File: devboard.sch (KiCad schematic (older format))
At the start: 91 parts, among them J1 Conn_01x04, J2 Conn_02x05_Odd_Even, J3 USB_B_Micro, J4 Conn_01x04, J5 Conn_02x10_Counter_Clockwise, J6 Conn_02x04_Counter_Clockwise, Q1 Q_NPN_BEC, Q2 Q_NPN_BEC, SW1 SW_SPST, U1 ATmega128L-8AU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

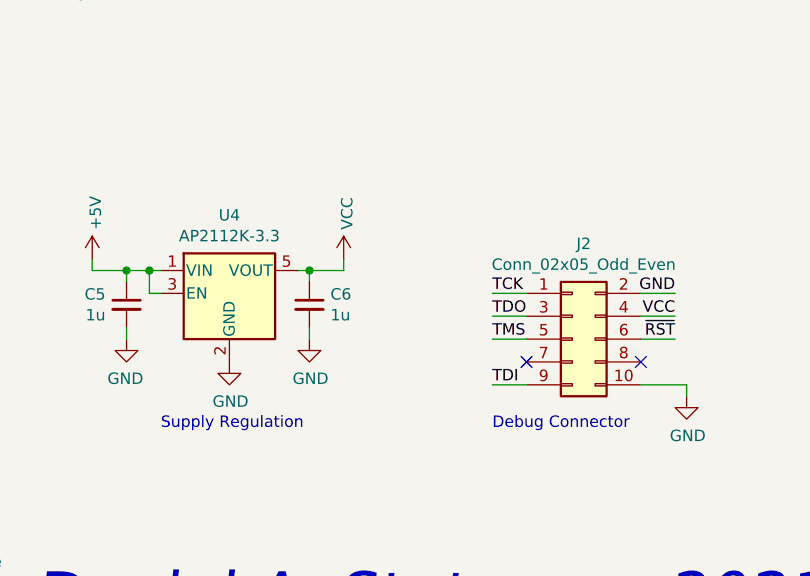
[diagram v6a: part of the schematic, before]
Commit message: Add power indicator and improve silk
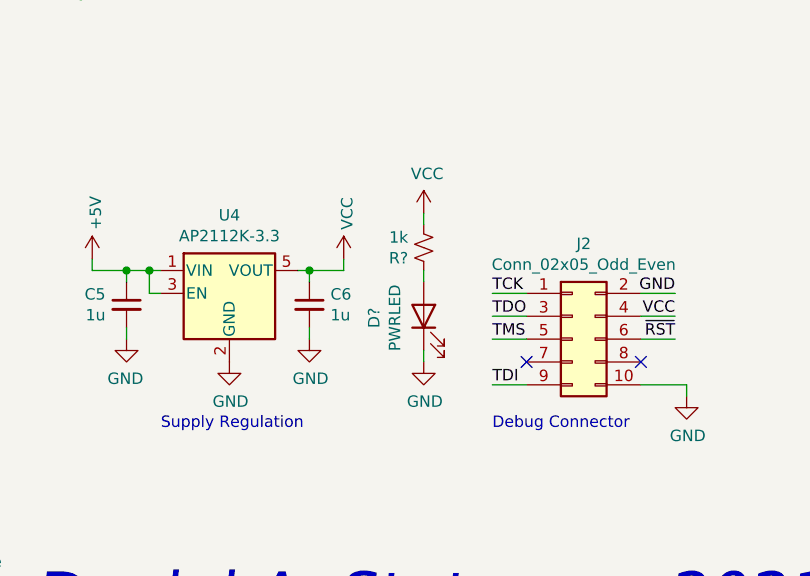
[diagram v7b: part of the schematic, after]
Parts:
- added D?: PWRLED, LED_SMD:LED_0603_1608Metric_Castellated, symbol Device:LED
- added R?: 1k, Resistor_SMD:R_0603_1608Metric_Pad0.98x0.95mm_HandSolder, symbol Device:R_Small_US
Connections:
- net GND: now also D?.1 (K)
- net VCC: now also R?.2
- new net: D?.2 (A), R?.1
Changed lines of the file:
@@
 Wire Wire Line
 	7850 4700 7850 4850
+Connection ~ 7850 4850
+Wire Wire Line
+	7850 4850 8200 4850
+$Comp
+L Device:R_Small_US R?
+U 1 1 60218294
+P 13600 8750
+F 0 "R?" H 13668 8796 50  0000 L CNN
+F 1 "1k" H 13668 8705 50  0000 L CNN
+F 2 "Resistor_SMD:R_0603_1608Metric_Pad0.98x0.95mm_HandSolder" H 13600 8750 50  0001 C CNN
+F 3 "~" H 13600 8750 50  0001 C CNN
+	1    13600 8750
+	-1   0    0    1
+$EndComp
+$Comp
+L power:GND #PWR?
+U 1 1 6028ABB4
+P 13600 9250
+F 0 "#PWR?" H 13600 9000 50  0001 C CNN
+F 1 "GND" H 13605 9077 50  0000 C CNN
+F 2 "" H 13600 9250 50  0001 C CNN
+F 3 "" H 13600 9250 50  0001 C CNN
+	1    13600 9250
+	1    0    0    -1
+$EndComp
+$Comp
+L Device:LED D?
+U 1 1 6021828E
+P 13600 9050
+F 0 "D?" H 13593 9267 50  0000 C CNN
+F 1 "PWRLED" H 13593 9176 50  0000 C CNN
+F 2 "LED_SMD:LED_0603_1608Metric_Castellated" H 13600 9050 50  0001 C CNN
+F 3 "~" H 13600 9050 50  0001 C CNN
+	1    13600 9050
+	0    -1   -1   0
+$EndComp
+Wire Wire Line
+	13600 9200 13600 9250
+Wire Wire Line
+	13600 8850 13600 8900
+$Comp
+L power:VCC #PWR?
+U 1 1 6053403F
+P 13600 8600
+F 0 "#PWR?" H 13600 8450 50  0001 C CNN
+F 1 "VCC" H 13615 8773 50  0000 C CNN
+F 2 "" H 13600 8600 50  0001 C CNN
+F 3 "" H 13600 8600 50  0001 C CNN
+	1    13600 8600
+	1    0    0    -1
+$EndComp
+Wire Wire Line
+	13600 8600 13600 8650
 Wire Bus Line
 	11700 10350 11700 10750
@@
 Wire Bus Line
 	8200 5450 8200 7500
-Connection ~ 7850 4850
-Wire Wire Line
-	7850 4850 8200 4850
 $EndSCHEMATC

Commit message: Annotation update
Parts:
- gave numbers to parts that had none: 2
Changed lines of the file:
@@
 	7850 4850 8200 4850
 $Comp
-L Device:R_Small_US R?
+L Device:R_Small_US R13
 U 1 1 60218294
 P 13600 8750
-F 0 "R?" H 13668 8796 50  0000 L CNN
+F 0 "R13" H 13668 8796 50  0000 L CNN
 F 1 "1k" H 13668 8705 50  0000 L CNN
 F 2 "Resistor_SMD:R_0603_1608Metric_Pad0.98x0.95mm_HandSolder" H 13600 8750 50  0001 C CNN
@@
 $EndComp
 $Comp
-L power:GND #PWR?
+L power:GND #PWR0122
 U 1 1 6028ABB4
 P 13600 9250
-F 0 "#PWR?" H 13600 9000 50  0001 C CNN
+F 0 "#PWR0122" H 13600 9000 50  0001 C CNN
 F 1 "GND" H 13605 9077 50  0000 C CNN
 F 2 "" H 13600 9250 50  0001 C CNN
@@
 $EndComp
 $Comp
-L Device:LED D?
+L Device:LED D11
 U 1 1 6021828E
 P 13600 9050
-F 0 "D?" H 13593 9267 50  0000 C CNN
+F 0 "D11" H 13593 9267 50  0000 C CNN
 F 1 "PWRLED" H 13593 9176 50  0000 C CNN
 F 2 "LED_SMD:LED_0603_1608Metric_Castellated" H 13600 9050 50  0001 C CNN
@@
 	13600 8850 13600 8900
 $Comp
-L power:VCC #PWR?
+L power:VCC #PWR0124
 U 1 1 6053403F
 P 13600 8600
-F 0 "#PWR?" H 13600 8450 50  0001 C CNN
+F 0 "#PWR0124" H 13600 8450 50  0001 C CNN
 F 1 "VCC" H 13615 8773 50  0000 C CNN
 F 2 "" H 13600 8600 50  0001 C CNN
